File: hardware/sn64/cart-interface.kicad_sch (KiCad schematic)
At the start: 85 parts, among them Q201 2N7002, U201 SN74LVC4245APWR, U202 SN74LVC4245APWR, U203 SN74LVC4245APWR, U204 SN74LVC4245APWR, U205 SN74LVC4245APWR, U206 SN74LVC4245APWR, U207 SN74LVC4245APWR, U209 SN74LVC244APWR, U210 SN74LVC1G07DBVR, U211 SN74LVC1G07DBVR, U212 SN74LVC1G07DBVR, U213 SN74LVC1G06DBVR, U214 SN74LVC1G06DBVR, U215 SN74LVC1T45DBVR, U216 SN74LVC1T45DBVR

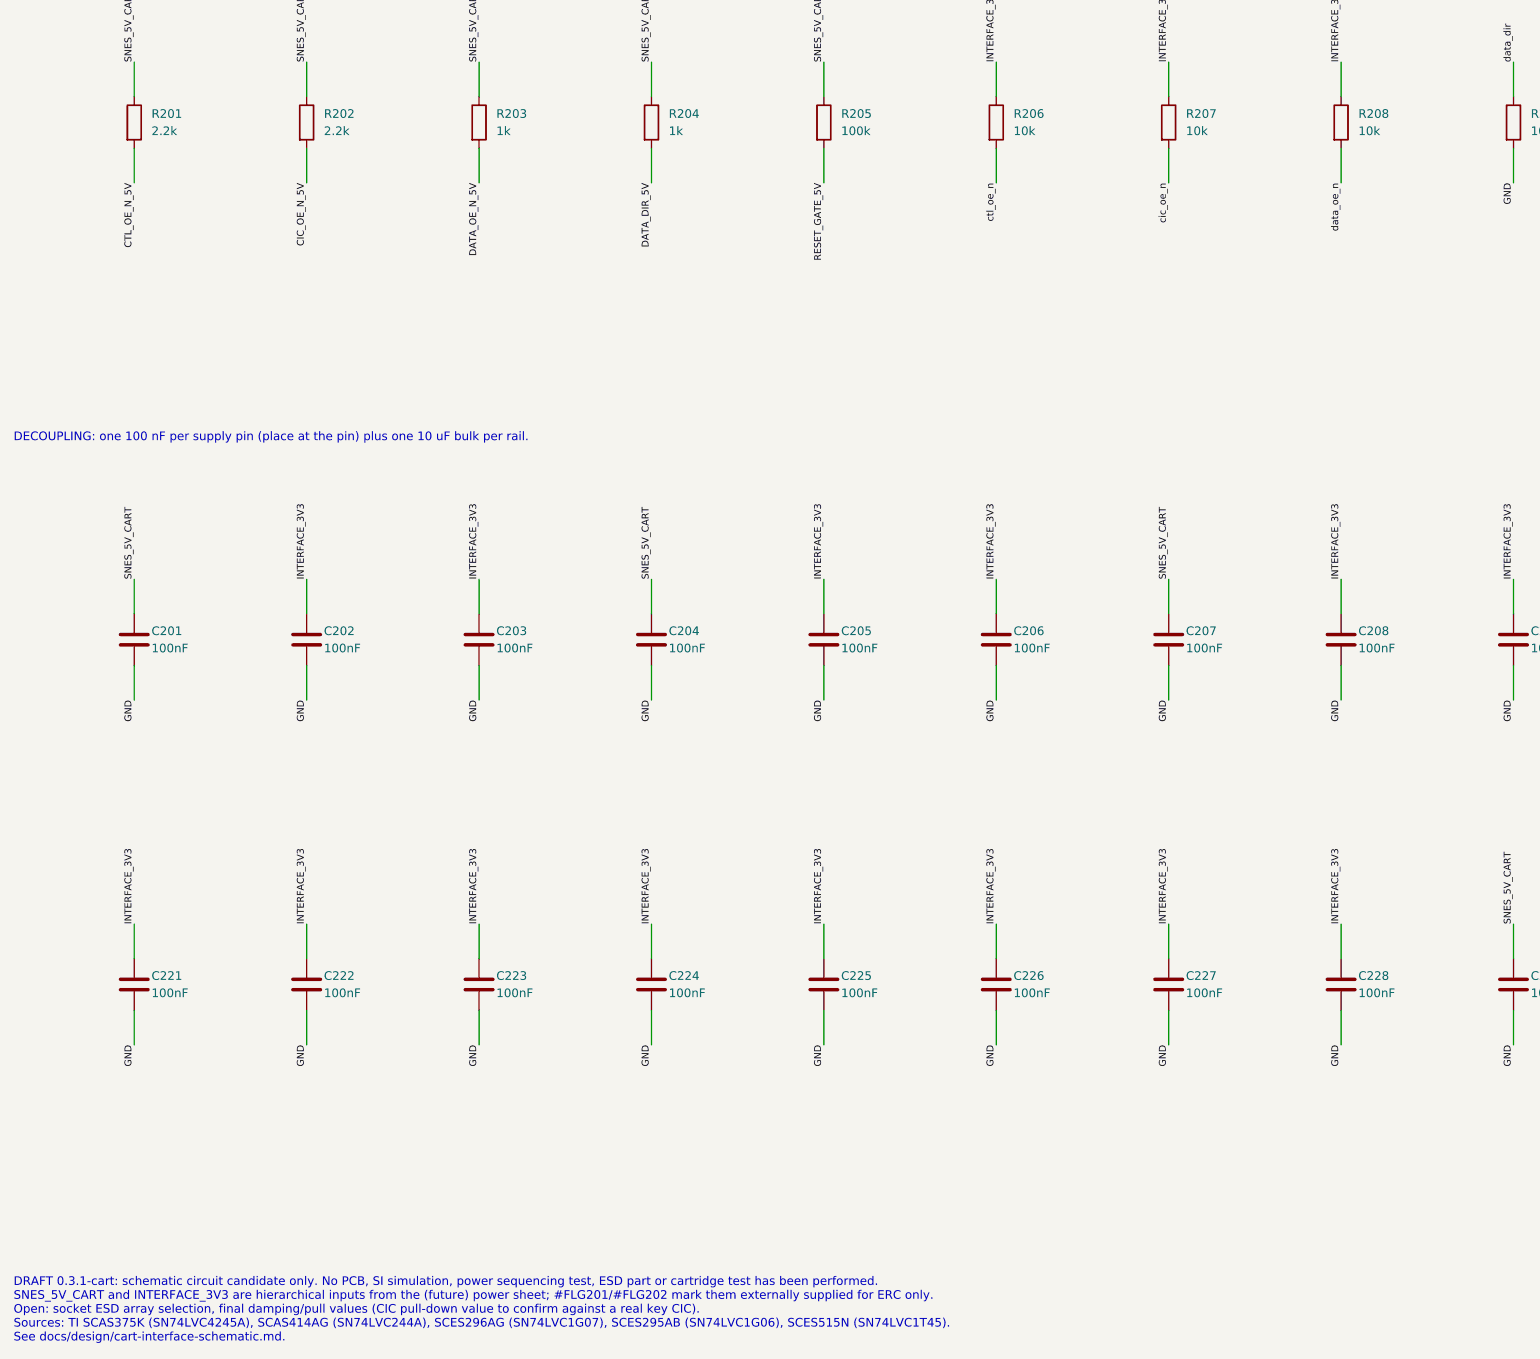
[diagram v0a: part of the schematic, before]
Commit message: Complete schematic draft: FPGA, power, clock/HDMI/audio sheets; PAL HDMI; cart audio
- New child sheets attached and wired at the root: FPGA (all 381 balls,
  W25Q128JV config flash, JTAG to the USB programmer, N64 edge through
  host-gated bus switches), power (priority-muxed host/USB eFuses, TUSB320
  permission, TPS63070 5V_PRE, FPGA bucks, cartridge eFuse and monitors),
  clock/HDMI/audio (Si5351A, TPD12S016 HDMI, PCM1808 cartridge-audio ADC).
- Real pinout: fpga/constraints/sn64_board.lpf; board top routed with it,
  all five clocks pass (SNES 28.9 MHz vs 21.48 required).
- PAL HDMI 576p50 frame-locked to the PAL SNES; Si5351 CLK2 retargeted only
  while the SNES clock is stopped. Cartridge audio mixed into HDMI.
  REGION_INFO/REGION_SOURCE mailbox telemetry shown in the menu.
  tb_system runs NTSC default, PAL header, PAL key and NTSC key.
- Safety fixes: efuse_fault_n pulled up to FPGA_3V3 (a 5V_PRE divider would
  back-drive a non-hot-socket bank); cart enable pull-ups 10k -> 4.7k
  (ECP5 config-time pull-down up to 150 uA).
- Checks: ERC 0 errors; interfaces 30/30, USB 69/69, cart 20/20, FPGA 13/13,
  power 23/23, A/V 30/30, root connectivity 4/4, all negative tests caught;
  evaluate.py --mode sim passes.

Co-Authored-By: Claude Fable 5.1 <noreply@anthropic.com>
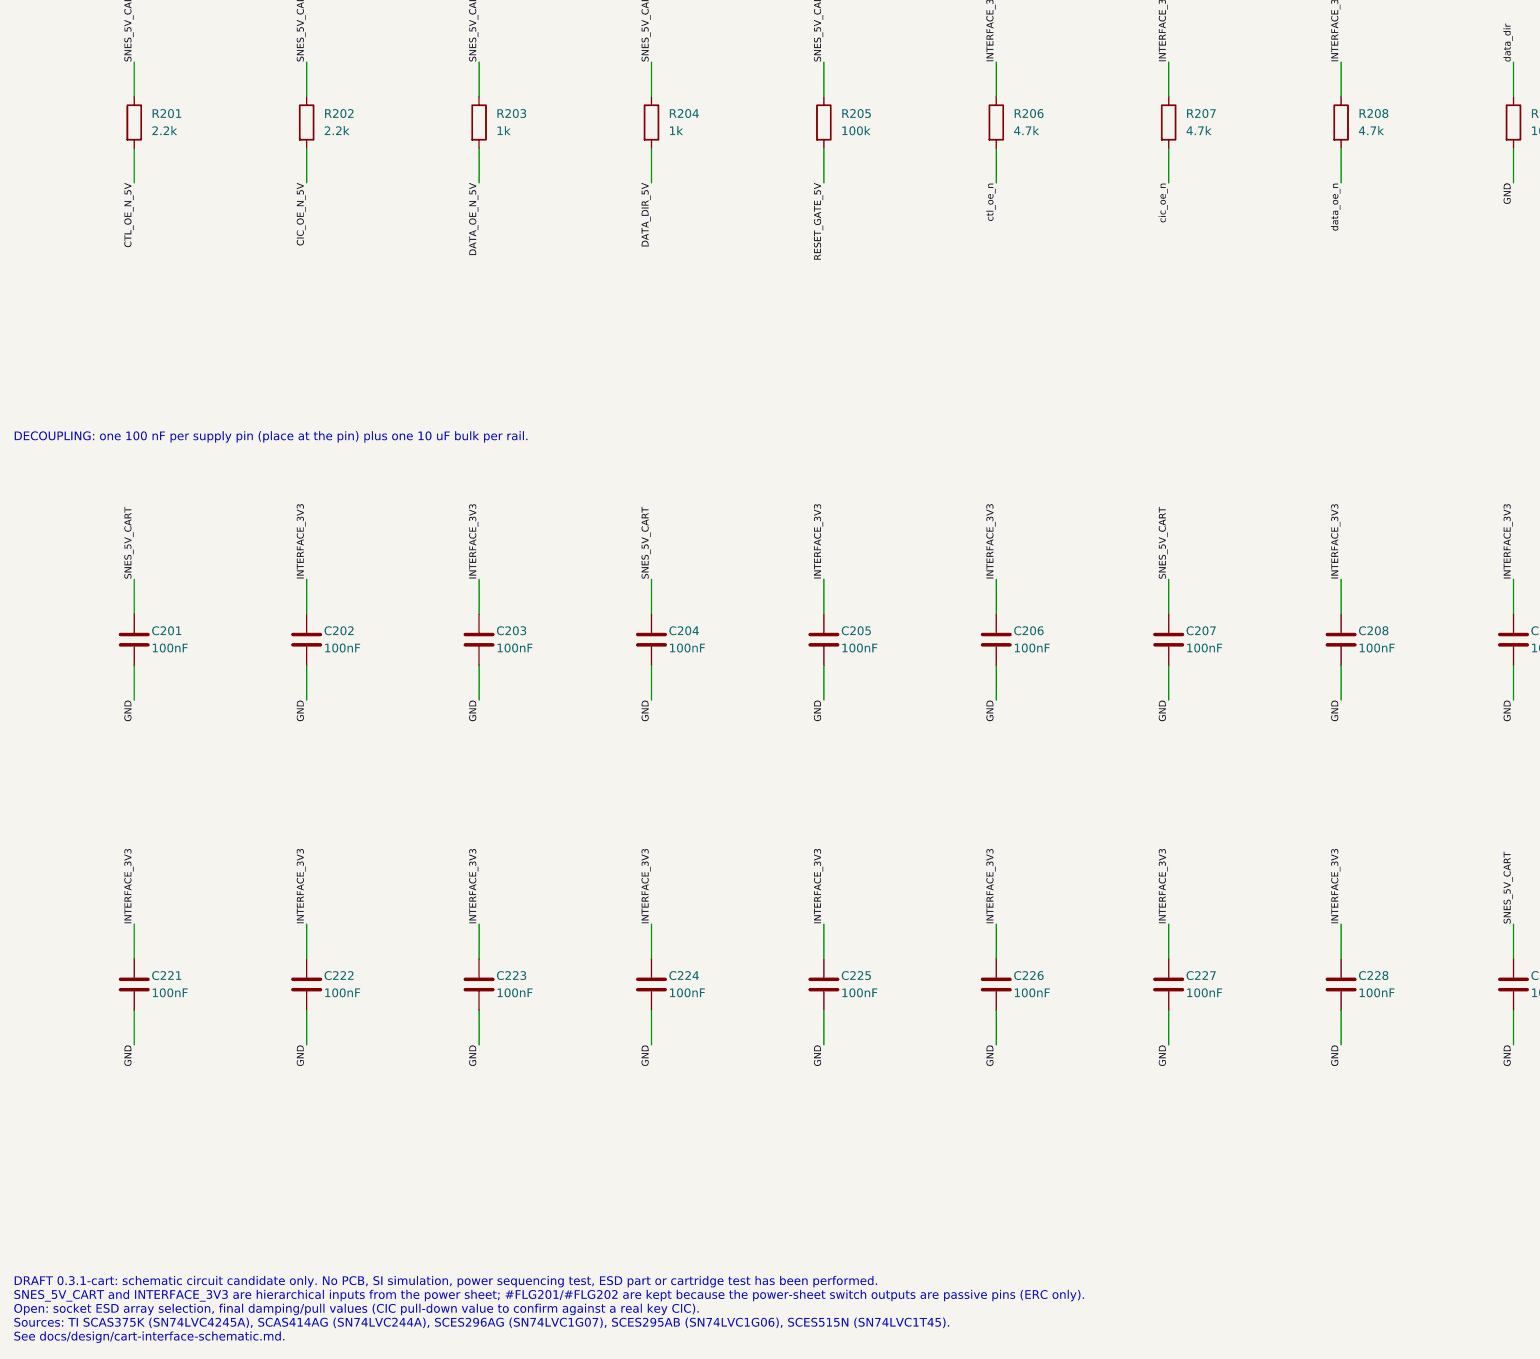
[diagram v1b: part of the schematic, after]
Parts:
- R206, R207, R208: value 10k -> 4.7k
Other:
- note added: "DRAFT 0.3.1-cart: schematic circuit candidate only. No PCB, SI simulation, power sequencing test, ESD part or cartridge test has been performed. SNES_5V_CART and INTERFACE_3V3 are hierarchical inputs from the power sheet; #FLG201/#FLG202 are kept because the power-sheet switch outputs are passive pins (ERC only). Open: socket ESD array selection, final damping/pull values (CIC pull-down value to 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"
- note removed: "DRAFT 0.3.1-cart: schematic circuit candidate only. No PCB, SI simulation, power sequencing test, ESD part or cartridge test has been performed. SNES_5V_CART and INTERFACE_3V3 are hierarchical inputs from the (future) power sheet; #FLG201/#FLG202 mark them externally supplied for ERC only. Open: socket ESD array selection, final damping/pull values (CIC pull-down value to confirm against a real k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"
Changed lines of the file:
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@@
 (symbol (lib_id "Device:R") (at 165.1 355.6 0) (unit 1) (exclude_from_sim no) (in_bom yes) (on_board yes) (dnp no)
 (property "Reference" "R206" (at 167.64 354.33 0) (effects (font (size 1.27 1.27)) (justify left)))
-(property "Value" "10k" (at 167.64 356.87 0) (effects (font (size 1.27 1.27)) (justify left)))
+(property "Value" "4.7k" (at 167.64 356.87 0) (effects (font (size 1.27 1.27)) (justify left)))
 (property "Footprint" "Resistor_SMD:R_0603_1608Metric" (at 165.1 355.6 0) (effects (font (size 1.27 1.27)) (hide yes)))
 (property "Datasheet" "" (at 165.1 355.6 0) (effects (font (size 1.27 1.27)) (hide yes)))
@@
 (symbol (lib_id "Device:R") (at 190.5 355.6 0) (unit 1) (exclude_from_sim no) (in_bom yes) (on_board yes) (dnp no)
 (property "Reference" "R207" (at 193.04 354.33 0) (effects (font (size 1.27 1.27)) (justify left)))
-(property "Value" "10k" (at 193.04 356.87 0) (effects (font (size 1.27 1.27)) (justify left)))
+(property "Value" "4.7k" (at 193.04 356.87 0) (effects (font (size 1.27 1.27)) (justify left)))
 (property "Footprint" "Resistor_SMD:R_0603_1608Metric" (at 190.5 355.6 0) (effects (font (size 1.27 1.27)) (hide yes)))
 (property "Datasheet" "" (at 190.5 355.6 0) (effects (font (size 1.27 1.27)) (hide yes)))
@@
 (symbol (lib_id "Device:R") (at 215.9 355.6 0) (unit 1) (exclude_from_sim no) (in_bom yes) (on_board yes) (dnp no)
 (property "Reference" "R208" (at 218.44 354.33 0) (effects (font (size 1.27 1.27)) (justify left)))
-(property "Value" "10k" (at 218.44 356.87 0) (effects (font (size 1.27 1.27)) (justify left)))
+(property "Value" "4.7k" (at 218.44 356.87 0) (effects (font (size 1.27 1.27)) (justify left)))
 (property "Footprint" "Resistor_SMD:R_0603_1608Metric" (at 215.9 355.6 0) (effects (font (size 1.27 1.27)) (hide yes)))
 (property "Datasheet" "" (at 215.9 355.6 0) (effects (font (size 1.27 1.27)) (hide yes)))
@@
 (text "HIERARCHICAL PORTS - CARTRIDGE SIDE (root J2 net labels)" (at 543.56 317.5 0) (effects (font (size 1.524 1.524)) (justify left top)))
 (text "PENDING PORTS - FPGA SIDE (bridge port names) + DEFAULT-OFF RAILS FROM FUTURE POWER SHEET" (at 690.88 317.5 0) (effects (font (size 1.524 1.524)) (justify left top)))
-(text "DRAFT 0.3.1-cart: schematic circuit candidate only. No PCB, SI simulation, power sequencing test, ESD part or cartridge test has been performed.\nSNES_5V_CART and INTERFACE_3V3 are hierarchical inputs from the (future) power sheet; #FLG201/#FLG202 mark them externally supplied for ERC only.\nOpen: socket ESD array selection, final damping/pull values (CIC pull-down value to confirm against a real key CIC).\nSources: TI SCAS375K (SN74LVC4245A), SCAS414AG (SN74LVC244A), SCES296AG (SN74LVC1G07), SCES295AB (SN74LVC1G06), SCES515N (SN74LVC1T45).\nSee docs/design/cart-interface-schematic.md." (at 20.32 525.78 0) (effects (font (size 1.27 1.27)) (justify left top)))
+(text "DRAFT 0.3.1-cart: schematic circuit candidate only. No PCB, SI simulation, power sequencing test, ESD part or cartridge test has been performed.\nSNES_5V_CART and INTERFACE_3V3 are hierarchical inputs from the power sheet; #FLG201/#FLG202 are kept because the power-sheet switch outputs are passive pins (ERC only).\nOpen: socket ESD array selection, final damping/pull values (CIC pull-down value to confirm against a real key CIC).\nSources: TI SCAS375K (SN74LVC4245A), SCAS414AG (SN74LVC244A), SCES296AG (SN74LVC1G07), SCES295AB (SN74LVC1G06), SCES515N (SN74LVC1T45).\nSee docs/design/cart-interface-schematic.md." (at 20.32 525.78 0) (effects (font (size 1.27 1.27)) (justify left top)))
 (sheet_instances (path "/e2505a21-9627-547b-aef4-ab0d2c57bd10/2176e4e6-adfa-5800-a82d-fd9d5a866057" (page "3"))) (embedded_fonts no))
